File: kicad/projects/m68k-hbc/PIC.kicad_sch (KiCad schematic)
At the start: 12 parts, among them J1 JTAG_PIC, U8 EPM7128SLC84 / Programmable I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, X5 70M

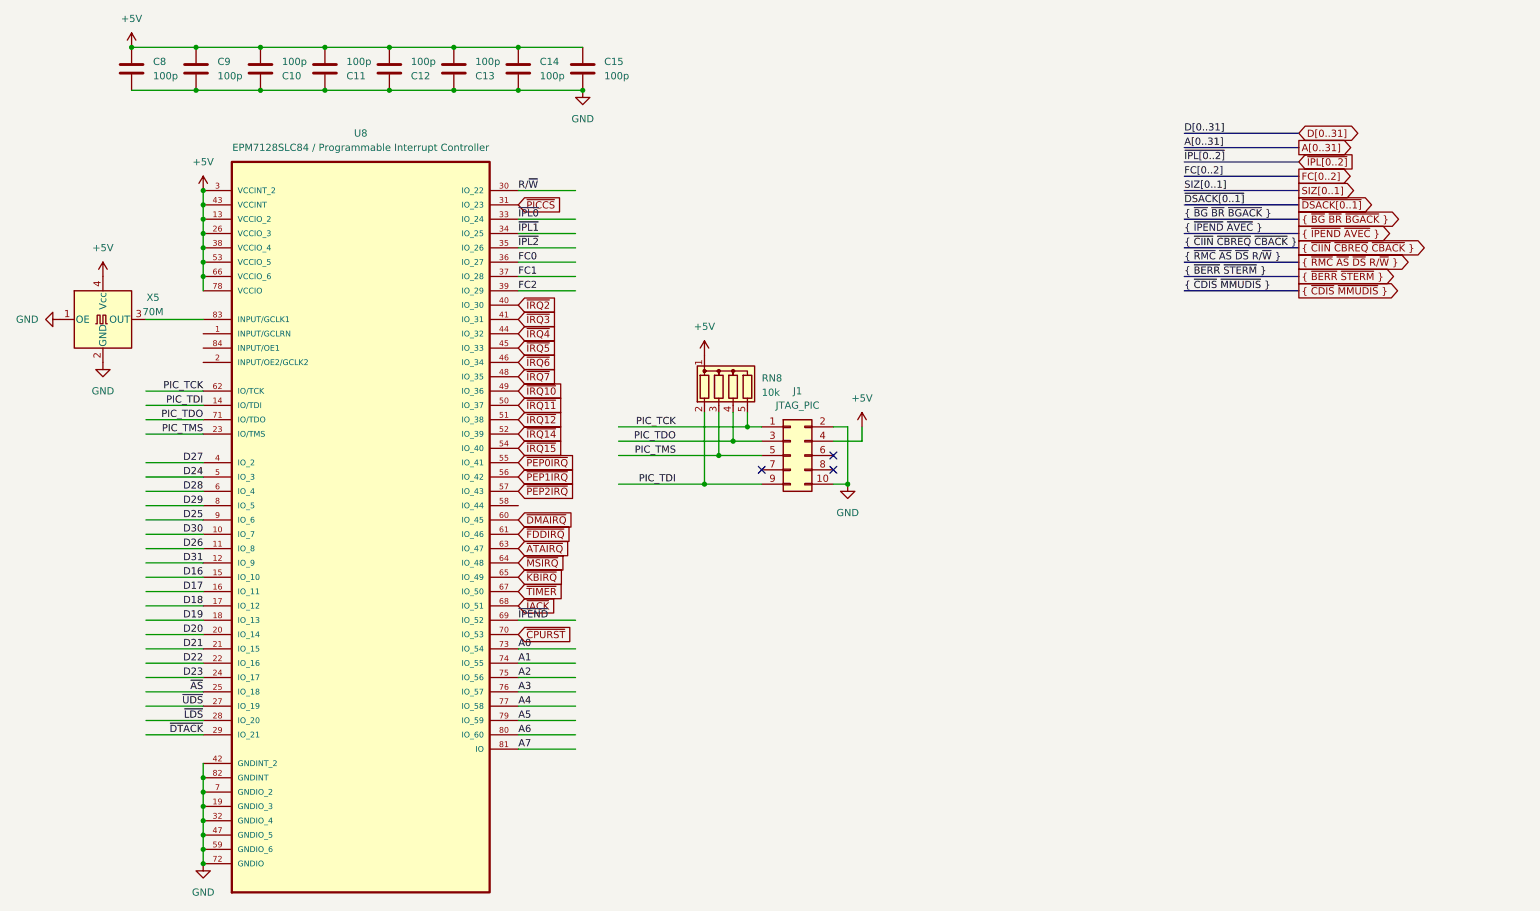
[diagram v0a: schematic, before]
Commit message: Modified system architecture, New KiCad Project: Cache Memory Module(SIMM80)
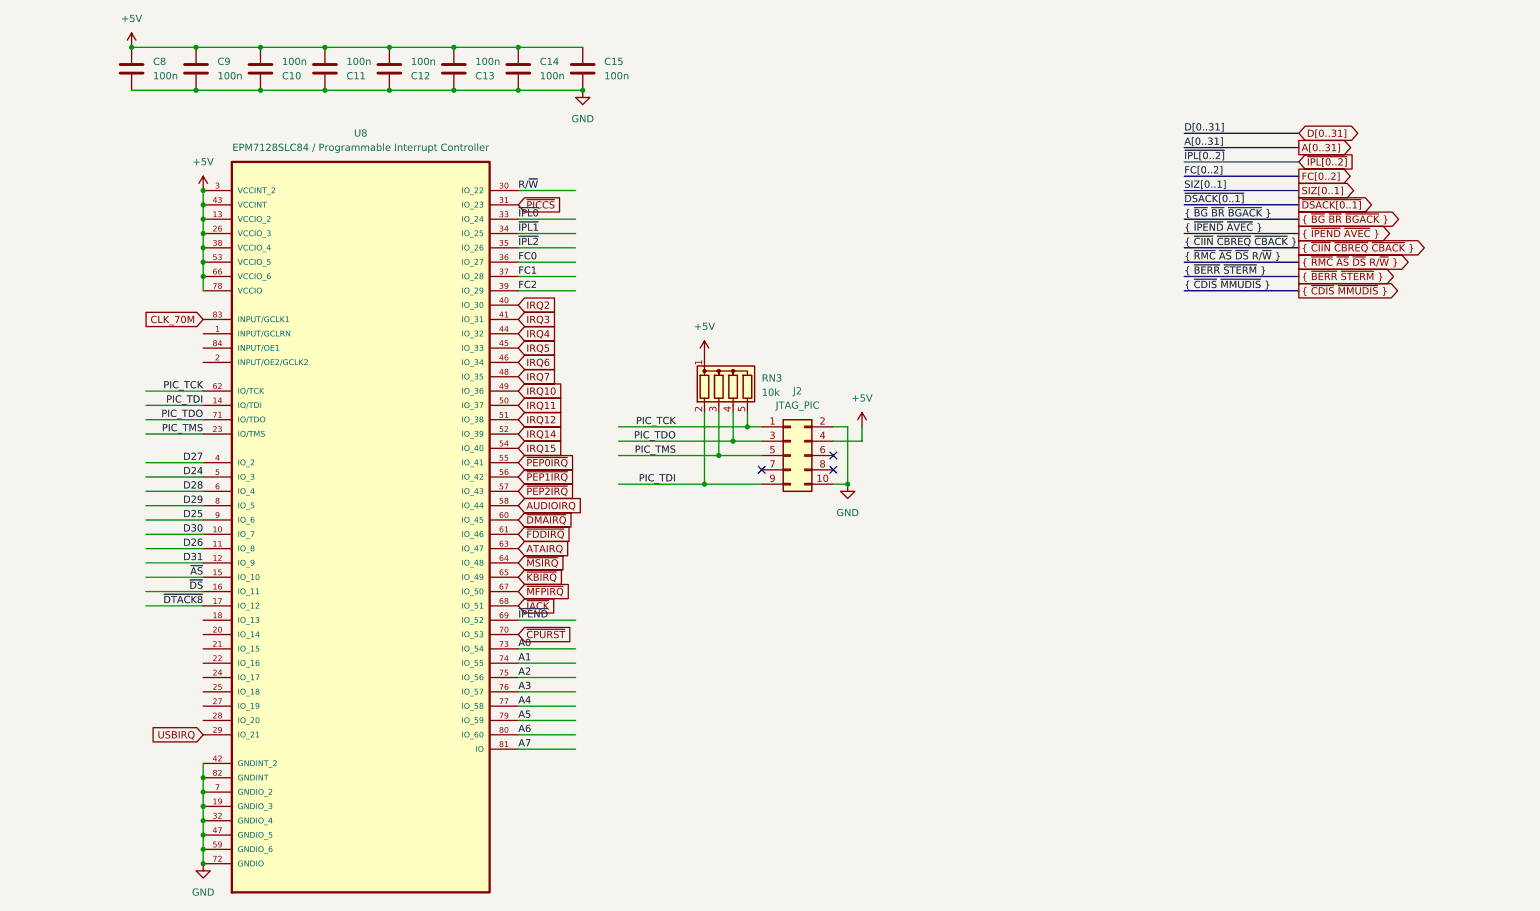
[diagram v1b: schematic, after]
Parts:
- removed X5: 70M, Oscillator:Oscillator_SMD_SeikoEpson_SG8002CA-4Pin_7.0x5.0mm, symbol Oscillator:SG-8002CA
- C10, C11, C12, C13, C14, C15, C8, C9: value 100p -> 100n
- renumbered J1 to J2, RN8 to RN3
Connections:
- net D16 is gone; now on net ~{AS}: U8.15 (IO_10)
- net ~{AS}: no longer U8.25 (IO_18)
- net CLK_70M: now reaches U8.83 (INPUT/GCLK1)
- net AUDIOIRQ: now reaches U8.58 (IO_44)
- net D17 renamed ~{DS}
- net D18 renamed ~{DTACK8}
- net D19: no longer names the net of U8.18 (IO_13)
- net D20: no longer names the net of U8.20 (IO_14)
- net D21: no longer names the net of U8.21 (IO_15)
- net D22: no longer names the net of U8.22 (IO_16)
- net D23: no longer names the net of U8.24 (IO_17)
- net ~{ATAIRQ} renamed ATAIRQ
- net ~{DTACK} renamed USBIRQ
- net ~{IRQ10} renamed IRQ10
- net ~{IRQ11} renamed IRQ11
- net ~{IRQ12} renamed IRQ12
- net ~{IRQ14} renamed IRQ14
- net ~{IRQ15} renamed IRQ15
- net ~{IRQ2} renamed IRQ2
- net ~{IRQ3} renamed IRQ3
- net ~{IRQ4} renamed IRQ4
- net ~{IRQ5} renamed IRQ5
- net ~{IRQ6} renamed IRQ6
- net ~{IRQ7} renamed IRQ7
- net ~{LDS}: no longer names the net of U8.28 (IO_20)
- net ~{TIMER} renamed ~{MFPIRQ}
- net ~{UDS}: no longer names the net of U8.27 (IO_19)
